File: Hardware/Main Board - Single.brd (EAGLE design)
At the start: 86.4 x 73.7 mm, 89 parts, among them J1 MICROMOD-2222-C, J10 MICRO-SD-PUSH-PUSH-EXT-PIN, J2 Vertical Qwiic Connector, J4 QWIIC_RIGHT_ANGLE, J5 CORTEX_JTAG_DEBUG_MINIMUM_PTH, J6 MICROMOD_CARRIER, Q1 3.1A/30V/105mΩ, U2 MCP73831, U5 AP7361C-33

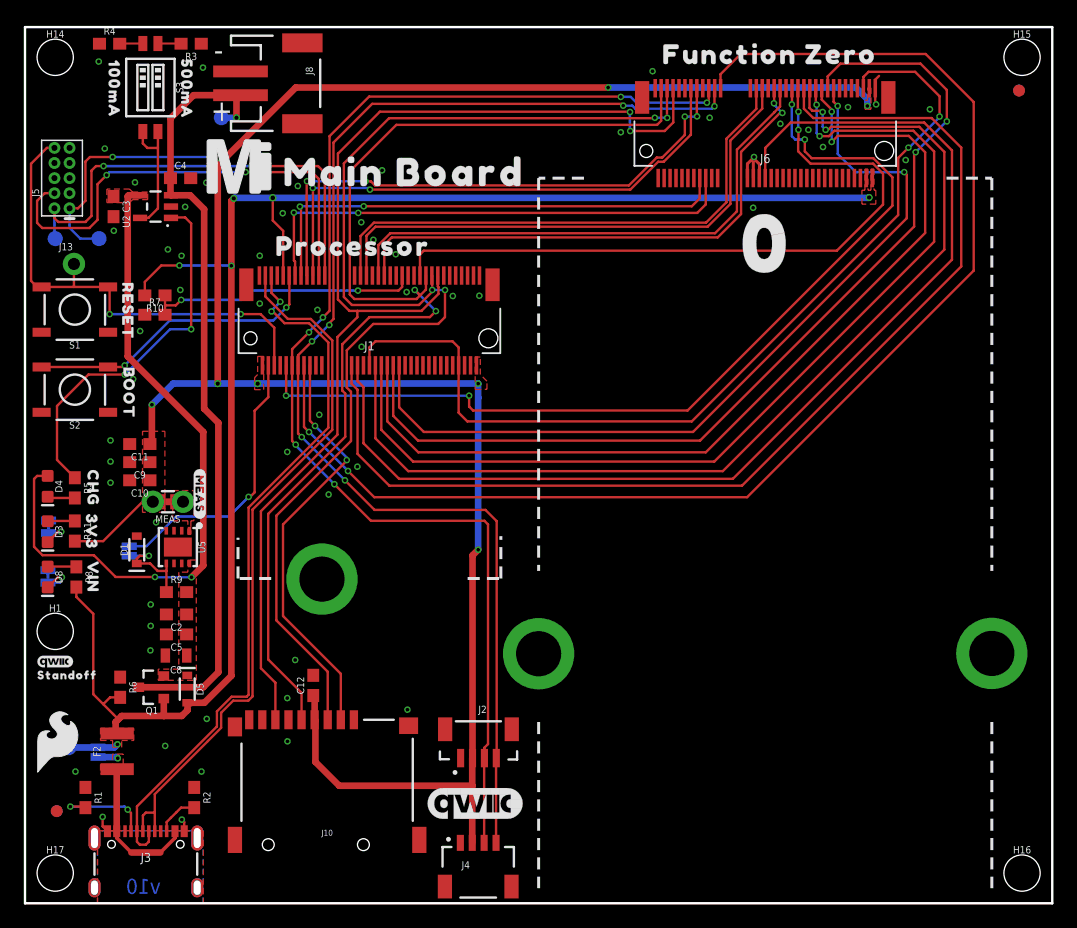
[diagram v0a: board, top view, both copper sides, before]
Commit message: Changes power to Function boards @ VCC to VCC and not VIN
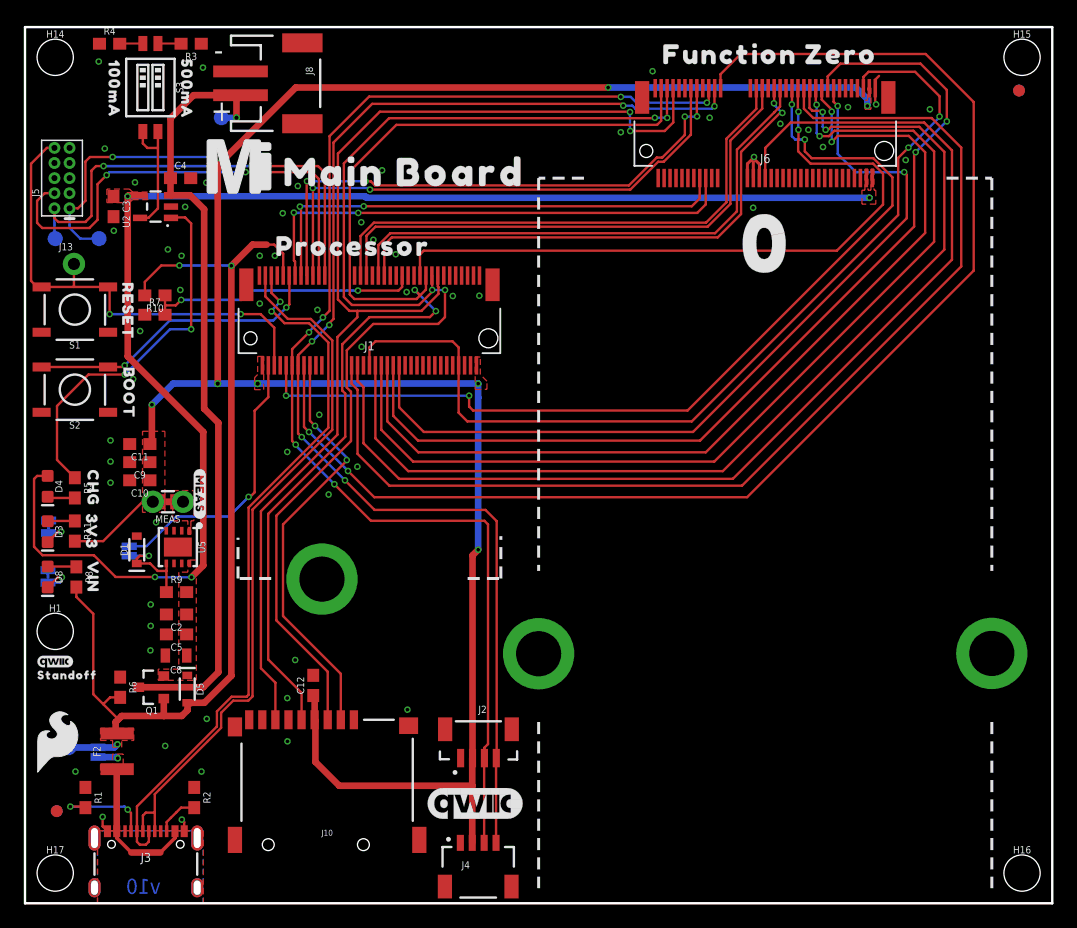
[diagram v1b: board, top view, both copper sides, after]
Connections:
- net VCC: now also J6.72, J6.74
- net VIN: no longer J6.72, J6.74
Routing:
- net VCC: track 57.4 -> 119.8 mm, vias 2 -> 4
- net VIN: track 142.2 -> 83.4 mm, vias 6 -> 3
- net GND: vias 59 -> 60
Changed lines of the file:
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@@
 <setting verticaltext="up"/>
 </settings>
-<grid distance="0.5" unitdist="mm" unit="mm" style="dots" multiple="1" display="yes" altdistance="0.01" altunitdist="mm" altunit="mm"/>
+<grid distance="0.05" unitdist="inch" unit="inch" style="dots" multiple="1" display="yes" altdistance="0.005" altunitdist="inch" altunit="inch"/>
 <layers>
 <layer number="1" name="Top" color="4" fill="1" visible="yes" active="yes"/>
@@
 <wire x1="71.48" y1="68.521" x2="71.48" y2="69.24" width="0.2032" layer="1"/>
 <wire x1="71.48" y1="69.24" x2="71.8" y2="69.56" width="0.2032" layer="1"/>
+<via x="21.0044" y="54.4368" extent="1-16" drill="0.3048"/>
 </signal>
 <signal name="V_BATT" class="1">
@@
 <contactref element="U2" pad="4"/>
 <contactref element="C3" pad="1"/>
-<wire x1="9.6727" y1="59.5224" x2="8.7224" y2="59.5224" width="0.5588" layer="1"/>
-<wire x1="8.7224" y1="59.5224" x2="8.636" y2="59.436" width="0.5588" layer="1"/>
+<wire x1="8.7224" y1="59.5224" x2="9.6727" y2="59.5224" width="0.5588" layer="1"/>
 <wire x1="8.636" y1="59.436" x2="8.636" y2="45.974" width="0.5588" layer="1"/>
 <wire x1="14.986" y1="39.624" x2="8.636" y2="45.974" width="0.5588" layer="1"/>
@@
 <contactref element="D5" pad="C"/>
 <contactref element="Q1" pad="2"/>
+<contactref element="J6" pad="72"/>
+<contactref element="J6" pad="74"/>
+<polygon width="0.127" layer="1" thermals="no">
+<vertex x="70.612" y="61.722"/>
+<vertex x="70.866" y="61.722"/>
+<vertex x="70.866" y="59.944"/>
+<vertex x="71.12" y="59.944"/>
+<vertex x="71.12" y="61.722"/>
+<vertex x="71.374" y="61.722"/>
+<vertex x="71.374" y="59.944"/>
+<vertex x="71.5264" y="59.944"/>
+<vertex x="71.5264" y="58.7756"/>
+<vertex x="70.358" y="58.7756"/>
+<vertex x="70.358" y="59.944"/>
+<vertex x="70.612" y="59.944"/>
+</polygon>
+<wire x1="8.7224" y1="59.5224" x2="8.636" y2="59.436" width="0.5588" layer="1"/>
+<via x="8.636" y="59.436" extent="1-16" drill="0.3048"/>
+<via x="70.993" y="59.309" extent="1-16" drill="0.3048"/>
+<wire x1="8.636" y1="59.436" x2="28.59413125" y2="59.436" width="0.5588" layer="16"/>
+<wire x1="28.59413125" y1="59.436" x2="28.71593125" y2="59.3142" width="0.5588" layer="16"/>
+<wire x1="70.9878" y1="59.3142" x2="70.993" y2="59.309" width="0.5588" layer="16"/>
+<wire x1="28.71593125" y1="59.3142" x2="70.9878" y2="59.3142" width="0.5588" layer="16"/>
 </signal>
 <signal name="D0-PROCESSOR">
@@
 <signal name="VIN">
 <contactref element="R10" pad="2"/>
-<contactref element="J6" pad="72"/>
-<contactref element="J6" pad="74"/>
 <wire x1="13.1826" y1="15.748" x2="13.6652" y2="16.2306" width="0.5588" layer="1"/>
-<via x="17.5514" y="59.2582" extent="1-16" drill="0.35"/>
-<wire x1="17.3482" y1="59.055" x2="17.3482" y2="53.594" width="0.5588" layer="1"/>
 <wire x1="17.3482" y1="19.1262" x2="17.3482" y2="53.594" width="0.5588" layer="1"/>
-<wire x1="17.3482" y1="59.055" x2="17.5514" y2="59.2582" width="0.5588" layer="1"/>
-<wire x1="17.5514" y1="59.2582" x2="17.6022" y2="59.309" width="0.5588" layer="16"/>
-<polygon width="0.127" layer="1" thermals="no">
-<vertex x="70.612" y="61.722"/>
-<vertex x="70.866" y="61.722"/>
-<vertex x="70.866" y="59.944"/>
-<vertex x="71.12" y="59.944"/>
-<vertex x="71.12" y="61.722"/>
-<vertex x="71.374" y="61.722"/>
-<vertex x="71.374" y="59.944"/>
-<vertex x="71.5264" y="59.944"/>
-<vertex x="71.5264" y="58.7756"/>
-<vertex x="70.358" y="58.7756"/>
-<vertex x="70.358" y="59.944"/>
-<vertex x="70.612" y="59.944"/>
-</polygon>
-<wire x1="17.6022" y1="59.309" x2="20.828" y2="59.309" width="0.5588" layer="16"/>
-<wire x1="20.828" y1="59.309" x2="70.9422" y2="59.309" width="0.5588" layer="16"/>
-<wire x1="70.9422" y1="59.309" x2="70.9676" y2="59.3344" width="0.5588" layer="16"/>
-<via x="70.9676" y="59.3344" extent="1-16" drill="0.35"/>
 <wire x1="10.072" y1="51.1048" x2="10.072" y2="52.236" width="0.2032" layer="1"/>
 <wire x1="11.4554" y1="53.6194" x2="12.9794" y2="53.6194" width="0.2032" layer="1"/>
@@
 <wire x1="7.62" y1="14.4032" x2="7.747" y2="14.2762" width="0.5588" layer="1"/>
 <wire x1="4.318" y1="26.582" x2="4.318" y2="25.7556" width="0.2032" layer="1"/>
-<wire x1="7.8486" y1="15.4686" x2="7.4041" y2="15.9131" width="0.2032" layer="1"/>
 <wire x1="4.318" y1="25.7556" x2="5.7404" y2="24.3332" width="0.2032" layer="1"/>
 <wire x1="5.7404" y1="24.3332" x2="5.7404" y2="17.5768" width="0.2032" layer="1"/>
 <contactref element="J1" pad="9"/>
-<wire x1="21.706" y1="52.773" x2="21.706" y2="56.526" width="0.2032" layer="1"/>
-<wire x1="21.706" y1="56.526" x2="20.828" y2="57.404" width="0.2032" layer="1"/>
-<wire x1="20.828" y1="57.404" x2="20.828" y2="59.309" width="0.2032" layer="1"/>
-<via x="20.828" y="59.309" extent="1-16" drill="0.381"/>
+<wire x1="21.706" y1="52.773" x2="21.706" y2="54.61" width="0.2032" layer="1"/>
 <polygon width="0.127" layer="1" isolate="0.3048" thermals="no">
 <vertex x="6.35" y="14.7066"/>
@@
 <contactref element="R6" pad="2"/>
 <wire x1="5.7404" y1="17.5768" x2="6.5786" y2="16.7386" width="0.2032" layer="1"/>
-<wire x1="6.5786" y1="16.7386" x2="7.4041" y2="15.9131" width="0.2032" layer="1"/>
+<wire x1="6.5786" y1="16.7386" x2="7.8486" y2="15.4686" width="0.2032" layer="1"/>
 <wire x1="6.5786" y1="16.7386" x2="7.151" y2="17.311" width="0.2032" layer="1"/>
 <wire x1="7.151" y1="17.311" x2="8.001" y2="17.311" width="0.2032" layer="1"/>
+<wire x1="17.3482" y1="53.594" x2="19.1262" y2="55.372" width="0.5588" layer="1"/>
+<wire x1="19.1262" y1="55.372" x2="20.32" y2="55.372" width="0.5588" layer="1"/>
+<wire x1="21.706" y1="54.61" x2="20.944" y2="55.372" width="0.2032" layer="1"/>
+<wire x1="20.944" y1="55.372" x2="20.32" y2="55.372" width="0.2032" layer="1"/>
 </signal>
 <signal name="SHLD">

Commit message: Rolls to V11
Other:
- board text added: "v11"
- board text removed: "v10"
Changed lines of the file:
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@@
 <wire x1="86.36" y1="73.66" x2="86.36" y2="0" width="0.2032" layer="20"/>
 <wire x1="0" y1="73.66" x2="0" y2="0" width="0.2032" layer="20"/>
-<text x="9.9568" y="1.4224" size="1.27" layer="16" font="vector" ratio="15" rot="MR0" align="center">v10</text>
+<text x="9.9568" y="1.4224" size="1.27" layer="16" font="vector" ratio="15" rot="MR0" align="center">v11</text>
 <text x="43.18" y="-25.654" size="1.778" layer="51" font="vector">Elias Santistevan</text>
 <text x="34.29" y="87.884" size="1.778" layer="47" font="vector" ratio="15">Units in Inches</text>

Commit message: Replaces shottky diode
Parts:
- D5: value 3A/10V/280mV -> 1A/23V/620mV
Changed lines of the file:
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@@
 <attribute name="VALUE" x="12.7" y="21.717" size="0.6096" layer="27" font="vector" ratio="20" rot="R180" align="top-center"/>
 </element>
-<element name="D5" library="SparkFun-DiscreteSemi" package="SOD-323" value="3A/10V/280mV" x="13.6398" y="18.0086" smashed="yes" rot="R270">
+<element name="D5" library="SparkFun-DiscreteSemi" package="SOD-323" value="1A/23V/620mV" x="13.6398" y="18.0086" smashed="yes" rot="R270">
 <attribute name="NAME" x="14.4018" y="18.0086" size="0.6096" layer="25" font="vector" ratio="20" rot="R270" align="bottom-center"/>
-<attribute name="PROD_ID" value="DIO-14072" x="-33.8582" y="57.3786" size="1.778" layer="27" rot="R270" display="off"/>
-<attribute name="VALUE" x="12.8778" y="18.0086" size="0.6096" layer="27" font="vector" ratio="20" rot="R270" align="top-center"/>
+<attribute name="PROD_ID" value="DIO-11623" x="-33.8582" y="57.3786" size="1.778" layer="27" rot="R270" display="off"/>
+<attribute name="VALUE" value="1A/23V/620mV" x="12.8778" y="18.0086" size="0.6096" layer="27" font="vector" ratio="20" rot="R270" align="top-center"/>
 </element>
 <element name="5V_LED" library="SparkFun-Jumpers" package="SMT-JUMPER_2_NC_TRACE_SILK" package3d_urn="urn:adsk.eagle:package:39281/1" value="" x="1.9304" y="27.4828" smashed="yes" rot="MR270">

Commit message: Updates function board symbol, fixes charging current value when 1 and 2 are flipped.
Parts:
- 3V3_LED, 5V_LED: value (none) -> JUMPER-SMT_2_NC_TRACE_SILK
- VE: value (none) -> JUMPER-SMT_2_NO_SILK
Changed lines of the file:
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@@
 <attribute name="VALUE" x="9.652" y="39.37" size="0.6096" layer="27" font="vector" ratio="20" rot="R180" align="top-center"/>
 </element>
-<element name="VE" library="SparkFun-Jumpers" package="SMT-JUMPER_2_NO_SILK" package3d_urn="urn:adsk.eagle:package:39279/1" value="" x="8.763" y="29.6164" smashed="yes" rot="MR270">
+<element name="VE" library="SparkFun-Jumpers" package="SMT-JUMPER_2_NO_SILK" package3d_urn="urn:adsk.eagle:package:39279/1" value="JUMPER-SMT_2_NO_SILK" x="8.763" y="29.6164" smashed="yes" rot="MR270">
 <attribute name="NAME" x="7.62" y="29.6164" size="0.6096" layer="26" font="vector" ratio="20" rot="MR270" align="bottom-center"/>
 <attribute name="VALUE" x="9.906" y="29.6164" size="0.6096" layer="28" font="vector" ratio="20" rot="MR270" align="top-center"/>
 </element>
-<element name="3V3_LED" library="SparkFun-Jumpers" package="SMT-JUMPER_2_NC_TRACE_SILK" package3d_urn="urn:adsk.eagle:package:39281/1" value="" x="1.9812" y="31.6484" smashed="yes" rot="MR270">
+<element name="3V3_LED" library="SparkFun-Jumpers" package="SMT-JUMPER_2_NC_TRACE_SILK" package3d_urn="urn:adsk.eagle:package:39281/1" value="JUMPER-SMT_2_NC_TRACE_SILK" x="1.9812" y="31.6484" smashed="yes" rot="MR270">
 <attribute name="NAME" x="0.8382" y="31.6484" size="0.6096" layer="26" font="vector" ratio="20" rot="MR270" align="bottom-center"/>
 <attribute name="VALUE" x="3.1242" y="31.6484" size="0.6096" layer="28" font="vector" ratio="20" rot="MR270" align="top-center"/>
@@
 <attribute name="VALUE" value="1A/23V/620mV" x="12.8778" y="18.0086" size="0.6096" layer="27" font="vector" ratio="20" rot="R270" align="top-center"/>
 </element>
-<element name="5V_LED" library="SparkFun-Jumpers" package="SMT-JUMPER_2_NC_TRACE_SILK" package3d_urn="urn:adsk.eagle:package:39281/1" value="" x="1.9304" y="27.4828" smashed="yes" rot="MR270">
+<element name="5V_LED" library="SparkFun-Jumpers" package="SMT-JUMPER_2_NC_TRACE_SILK" package3d_urn="urn:adsk.eagle:package:39281/1" value="JUMPER-SMT_2_NC_TRACE_SILK" x="1.9304" y="27.4828" smashed="yes" rot="MR270">
 <attribute name="NAME" x="0.7874" y="27.4828" size="0.6096" layer="26" font="vector" ratio="20" rot="MR270" align="bottom-center"/>
 <attribute name="VALUE" x="3.0734" y="27.4828" size="0.6096" layer="28" font="vector" ratio="20" rot="MR270" align="top-center"/>

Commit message: Updates the design to use the Micromod-function device in the official SFE Eagle Libs
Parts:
- J6: value MICROMOD_CARRIER -> MICROMOD_FUNCTION_MAIN; device SparkFun-MicroMod-Function:M.2-CONNECTOR-E-FUNCTION-STANDARD -> SparkFun-MicroMod:M.2-CONNECTOR-E-FUNCTION-STANDARD
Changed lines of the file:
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@@
 <?xml version="1.0" encoding="utf-8"?>
 <!DOCTYPE eagle SYSTEM "eagle.dtd">
-<eagle version="9.6.2">
+<eagle version="9.5.1">
 <drawing>
 <settings>
@@
 </layers>
 <board>
-<fusionsync huburn="a.YnVzaW5lc3M6c3BhcmtmdW4y" projecturn="a.YnVzaW5lc3M6c3BhcmtmdW4yI0QyMDIwMDIxMTI2NDY1MzM1MQ" f3durn="urn:adsk.wipprod:dm.lineage:JfmCBB-MQPmSslj1S-6PSg" pcbguid="" lastpulledtime="" lastsyncedchangeguid="" latestrevisionid="43284b18-0cc2-4a1f-8182-a2c436edfe4c" lastsyncedrevisionid="43284b18-0cc2-4a1f-8182-a2c436edfe4c" lastboardhashguid="23094fc8-4401-f022-9fbc-6be2b6996c0c" lastpushedtime="2021-07-22T19:41:21Z" linktopcb3d="true"/>
 <plain>
 <wire x1="86.36" y1="0" x2="0" y2="0" width="0.2032" layer="20"/>
@@
 <attribute name="VALUE" x="10.922" y="51.8668" size="0.6096" layer="27" font="vector" ratio="20" rot="R180" align="top-center"/>
 </element>
-<element name="J6" library="SparkFun-MicroMod-Function" package="M.2-CONNECTOR-E-FUNCTION-STANDARD" value="MICROMOD_CARRIER" x="62.23" y="63.246" smashed="yes" rot="R180">
+<element name="J6" library="SparkFun-MicroMod" package="M.2-CONNECTOR-E-FUNCTION-STANDARD" value="MICROMOD_FUNCTION_MAIN" x="62.23" y="63.246" smashed="yes" rot="R180">
 <attribute name="NAME" x="62.23" y="62.611" size="0.762" layer="25" rot="R180" align="center"/>
 <attribute name="PROD_ID" value="CONN-14877" x="62.23" y="63.246" size="1.778" layer="27" rot="R180" display="off"/>
@@
 <compatibility>
 <note version="8.3" severity="warning">
-Since Version 8.3, EAGLE supports Fusion synchronisation.
-This feature will not be available in this version and saving
-the document will break the link to the Fusion PCB feature.
-</note>
-<note version="8.3" severity="warning">
 Since Version 8.3, EAGLE supports URNs for individual library
